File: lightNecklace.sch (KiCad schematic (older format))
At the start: 68 parts

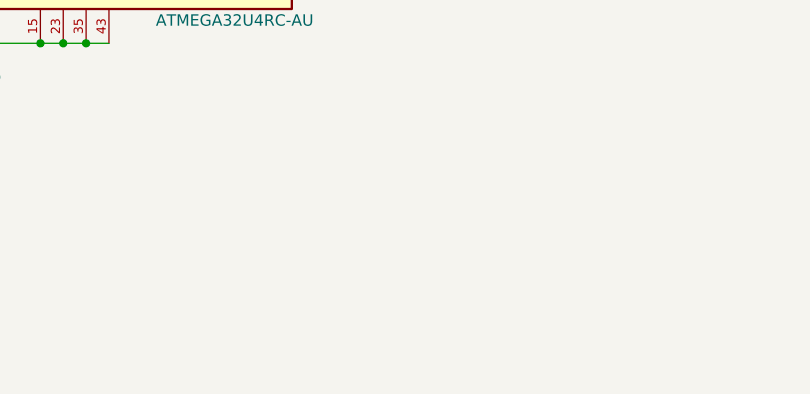
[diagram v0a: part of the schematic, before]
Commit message: Added treble cleff
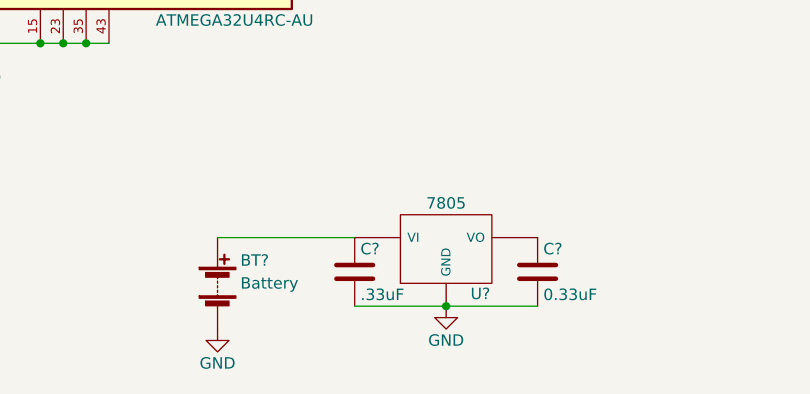
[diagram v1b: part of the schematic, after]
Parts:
- added BT?: Battery, symbol Battery
- added C?: .33uF, symbol C
- added C?: 0.33uF, symbol C
- added U?: 7805, symbol 7805
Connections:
- net GND: now also BT?.2 (-), C?.2, C?.2, U?.GND
- new net: BT?.1 (+), C?.1, U?.VI
- new net: C?.1, U?.VO
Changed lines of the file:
@@
 $EndComp
 NoConn ~ 1125 3625
-Wire Wire Line
-	1650 3325 1900 3325
-Wire Wire Line
-	1125 2925 1900 2925
-Wire Wire Line
-	1450 2625 1650 2625
-Wire Wire Line
-	1675 3025 1900 3025
-Wire Wire Line
-	1900 3025 1900 3075
-Wire Wire Line
-	1675 3225 1900 3225
-Wire Wire Line
-	1900 3225 1900 3175
-Wire Wire Line
-	2600 1475 2475 1475
-Wire Wire Line
-	2475 1475 2475 1175
-Wire Wire Line
-	2850 1475 2750 1475
-Wire Wire Line
-	2750 1475 2750 1175
-Wire Wire Line
-	2950 1475 3025 1475
-Wire Wire Line
-	3025 1475 3025 1175
-Wire Wire Line
-	3300 1475 3550 1475
-Wire Wire Line
-	3550 1475 3550 1175
-Wire Wire Line
-	2225 875  3550 875
-Connection ~ 3275 875
-Connection ~ 3025 875
-Connection ~ 2750 875
-Connection ~ 2475 875
-Connection ~ 3275 1175
-Wire Wire Line
-	3200 1475 3200 1350
-Wire Wire Line
-	3200 1350 3275 1350
-Wire Wire Line
-	3275 1350 3275 1175
-Wire Wire Line
-	3550 1175 1600 1175
-Connection ~ 3025 1175
-Connection ~ 2750 1175
-Connection ~ 2475 1175
-Wire Wire Line
-	1200 1725 1900 1725
-Wire Wire Line
-	1600 1175 1600 1425
-Connection ~ 1850 1175
-Connection ~ 1600 1725
-Wire Wire Line
-	1200 1525 1375 1525
-Wire Wire Line
-	700  1525 700  1525
-Wire Wire Line
-	700  1525 700  1350
-Wire Wire Line
-	700  1350 1375 1350
-Wire Wire Line
-	1375 1350 1375 1525
-Wire Wire Line
-	700  1725 700  1975
-Wire Wire Line
-	700  1975 1200 1975
-Wire Wire Line
-	1200 1975 1200 1725
-Wire Wire Line
-	525  2075 525  2650
-Connection ~ 525  2375
-Wire Wire Line
-	1900 2075 1900 2125
-Wire Wire Line
-	825  2075 1900 2075
-Wire Wire Line
-	1900 2375 1900 2325
-Wire Wire Line
-	825  2375 1900 2375
-Connection ~ 1175 2075
-Connection ~ 1175 2375
-Wire Wire Line
-	975  2225 525  2225
-Connection ~ 525  2225
-Wire Wire Line
-	1375 2225 1375 2175
-Wire Wire Line
-	1375 2175 1575 2175
-Wire Wire Line
-	1125 3425 1250 3425
-Wire Wire Line
-	1250 3425 1250 3025
-Wire Wire Line
-	1250 3025 1375 3025
-Wire Wire Line
-	1125 3525 1375 3525
-Wire Wire Line
-	1375 3525 1375 3225
-Wire Wire Line
-	1125 3225 1125 2925
-Connection ~ 1650 2925
-Wire Wire Line
-	725  3825 825  3825
-Connection ~ 775  3825
-Wire Wire Line
-	2650 4875 3200 4875
-Connection ~ 3000 4875
-Connection ~ 3100 4875
-Connection ~ 2900 4875
 $Comp
 L GND #PWR?
@@
 	0    1    1    0
 $EndComp
-Wire Wire Line
-	4150 1825 4600 1825
-Wire Wire Line
-	4150 1925 4600 1925
-Wire Wire Line
-	4150 2025 4600 2025
 Text Label 4150 1725 0    60   ~ 0
 LED1
@@
 Text Label 8650 4475 2    60   ~ 0
 LED25
+$Comp
+L GND #PWR?
+U 1 1 5A3F89C4
+P 7600 4775
+F 0 "#PWR?" H 7600 4525 50  0001 C CNN
+F 1 "GND" H 7600 4625 50  0000 C CNN
+F 2 "" H 7600 4775 50  0001 C CNN
+F 3 "" H 7600 4775 50  0001 C CNN
+	1    7600 4775
+	1    0    0    -1
+$EndComp
+$Comp
+L GND #PWR?
+U 1 1 5A3FA7AA
+P 9250 4475
+F 0 "#PWR?" H 9250 4225 50  0001 C CNN
+F 1 "GND" H 9250 4325 50  0000 C CNN
+F 2 "" H 9250 4475 50  0001 C CNN
+F 3 "" H 9250 4475 50  0001 C CNN
+	1    9250 4475
+	1    0    0    -1
+$EndComp
+$Comp
+L 7805 U?
+U 1 1 5A3FDDB3
+P 4675 5775
+F 0 "U?" H 4825 5579 50  0000 C CNN
+F 1 "7805" H 4675 5975 50  0000 C CNN
+F 2 "" H 4675 5775 50  0001 C CNN
+F 3 "" H 4675 5775 50  0001 C CNN
+	1    4675 5775
+	1    0    0    -1
+$EndComp
+$Comp
+L Battery BT?
+U 1 1 5A3FE745
+P 3675 5925
+F 0 "BT?" H 3775 6025 50  0000 L CNN
+F 1 "Battery" H 3775 5925 50  0000 L CNN
+F 2 "" V 3675 5985 50  0001 C CNN
+F 3 "" V 3675 5985 50  0001 C CNN
+	1    3675 5925
+	1    0    0    -1
+$EndComp
+$Comp
+L C C?
+U 1 1 5A3FEA3A
+P 4275 5875
+F 0 "C?" H 4300 5975 50  0000 L CNN
+F 1 ".33uF" H 4300 5775 50  0000 L CNN
+F 2 "" H 4313 5725 50  0001 C CNN
+F 3 "" H 4275 5875 50  0001 C CNN
+	1    4275 5875
+	1    0    0    -1
+$EndComp
+$Comp
+L C C?
+U 1 1 5A3FEB31
+P 5075 5875
+F 0 "C?" H 5100 5975 50  0000 L CNN
+F 1 "0.33uF" H 5100 5775 50  0000 L CNN
+F 2 "" H 5113 5725 50  0001 C CNN
+F 3 "" H 5075 5875 50  0001 C CNN
+	1    5075 5875
+	1    0    0    -1
+$EndComp
+$Comp
+L GND #PWR?
+U 1 1 5A4001D3
+P 4675 6025
+F 0 "#PWR?" H 4675 5775 50  0001 C CNN
+F 1 "GND" H 4675 5875 50  0000 C CNN
+F 2 "" H 4675 6025 50  0001 C CNN
+F 3 "" H 4675 6025 50  0001 C CNN
+	1    4675 6025
+	1    0    0    -1
+$EndComp
+$Comp
+L GND #PWR?
+U 1 1 5A40034F
+P 3675 6125
+F 0 "#PWR?" H 3675 5875 50  0001 C CNN
+F 1 "GND" H 3675 5975 50  0000 C CNN
+F 2 "" H 3675 6125 50  0001 C CNN
+F 3 "" H 3675 6125 50  0001 C CNN
+	1    3675 6125
+	1    0    0    -1
+$EndComp
+Wire Wire Line
+	1650 3325 1900 3325
+Wire Wire Line
+	1125 2925 1900 2925
+Wire Wire Line
+	1450 2625 1650 2625
+Wire Wire Line
+	1675 3025 1900 3025
+Wire Wire Line
+	1900 3025 1900 3075
+Wire Wire Line
+	1675 3225 1900 3225
+Wire Wire Line
+	1900 3225 1900 3175
+Wire Wire Line
+	2600 1475 2475 1475
+Wire Wire Line
+	2475 1475 2475 1175
+Wire Wire Line
+	2850 1475 2750 1475
+Wire Wire Line
+	2750 1475 2750 1175
+Wire Wire Line
+	2950 1475 3025 1475
+Wire Wire Line
+	3025 1475 3025 1175
+Wire Wire Line
+	3300 1475 3550 1475
+Wire Wire Line
+	3550 1475 3550 1175
+Wire Wire Line
+	2225 875  3550 875
+Connection ~ 3275 875
+Connection ~ 3025 875
+Connection ~ 2750 875
+Connection ~ 2475 875
+Connection ~ 3275 1175
+Wire Wire Line
+	3200 1475 3200 1350
+Wire Wire Line
+	3200 1350 3275 1350
+Wire Wire Line
+	3275 1350 3275 1175
+Wire Wire Line
+	3550 1175 1600 1175
+Connection ~ 3025 1175
+Connection ~ 2750 1175
+Connection ~ 2475 1175
+Wire Wire Line
+	1200 1725 1900 1725
+Wire Wire Line
+	1600 1175 1600 1425
+Connection ~ 1850 1175
+Connection ~ 1600 1725
+Wire Wire Line
+	1200 1525 1375 1525
+Wire Wire Line
+	700  1525 700  1525
+Wire Wire Line
+	700  1525 700  1350
+Wire Wire Line
+	700  1350 1375 1350
+Wire Wire Line
+	1375 1350 1375 1525
+Wire Wire Line
+	700  1725 700  1975
+Wire Wire Line
+	700  1975 1200 1975
+Wire Wire Line
+	1200 1975 1200 1725
+Wire Wire Line
+	525  2075 525  2650
+Connection ~ 525  2375
+Wire Wire Line
+	1900 2075 1900 2125
+Wire Wire Line
+	825  2075 1900 2075
+Wire Wire Line
+	1900 2375 1900 2325
+Wire Wire Line
+	825  2375 1900 2375
+Connection ~ 1175 2075
+Connection ~ 1175 2375
+Wire Wire Line
+	975  2225 525  2225
+Connection ~ 525  2225
+Wire Wire Line
+	1375 2225 1375 2175
+Wire Wire Line
+	1375 2175 1575 2175
+Wire Wire Line
+	1125 3425 1250 3425
+Wire Wire Line
+	1250 3425 1250 3025
+Wire Wire Line
+	1250 3025 1375 3025
+Wire Wire Line
+	1125 3525 1375 3525
+Wire Wire Line
+	1375 3525 1375 3225
+Wire Wire Line
+	1125 3225 1125 2925
+Connection ~ 1650 2925
+Wire Wire Line
+	725  3825 825  3825
+Connection ~ 775  3825
+Wire Wire Line
+	2650 4875 3200 4875
+Connection ~ 3000 4875
+Connection ~ 3100 4875
+Connection ~ 2900 4875
+Wire Wire Line
+	4150 1825 4600 1825
+Wire Wire Line
+	4150 1925 4600 1925
+Wire Wire Line
+	4150 2025 4600 2025
 Wire Wire Line
 	7600 1475 7600 4775
@@
 Connection ~ 7600 4225
 Connection ~ 7600 4500
-$Comp
-L GND #PWR?
-U 1 1 5A3F89C4
-P 7600 4775
-F 0 "#PWR?" H 7600 4525 50  0001 C CNN
-F 1 "GND" H 7600 4625 50  0000 C CNN
-F 2 "" H 7600 4775 50  0001 C CNN
-F 3 "" H 7600 4775 50  0001 C CNN
-	1    7600 4775
-	1    0    0    -1
-$EndComp
 Wire Wire Line
 	9250 1450 9250 4475
@@
 Connection ~ 9250 3925
 Connection ~ 9250 4200
-$Comp
-L GND #PWR?
-U 1 1 5A3FA7AA
-P 9250 4475
-F 0 "#PWR?" H 9250 4225 50  0001 C CNN
-F 1 "GND" H 9250 4325 50  0000 C CNN
-F 2 "" H 9250 4475 50  0001 C CNN
-F 3 "" H 9250 4475 50  0001 C CNN
-	1    9250 4475
-	1    0    0    -1
-$EndComp
+Wire Wire Line
+	4275 6025 5075 6025
+Connection ~ 4675 6025
+Wire Wire Line
+	3675 5725 4275 5725
 $EndSCHEMATC

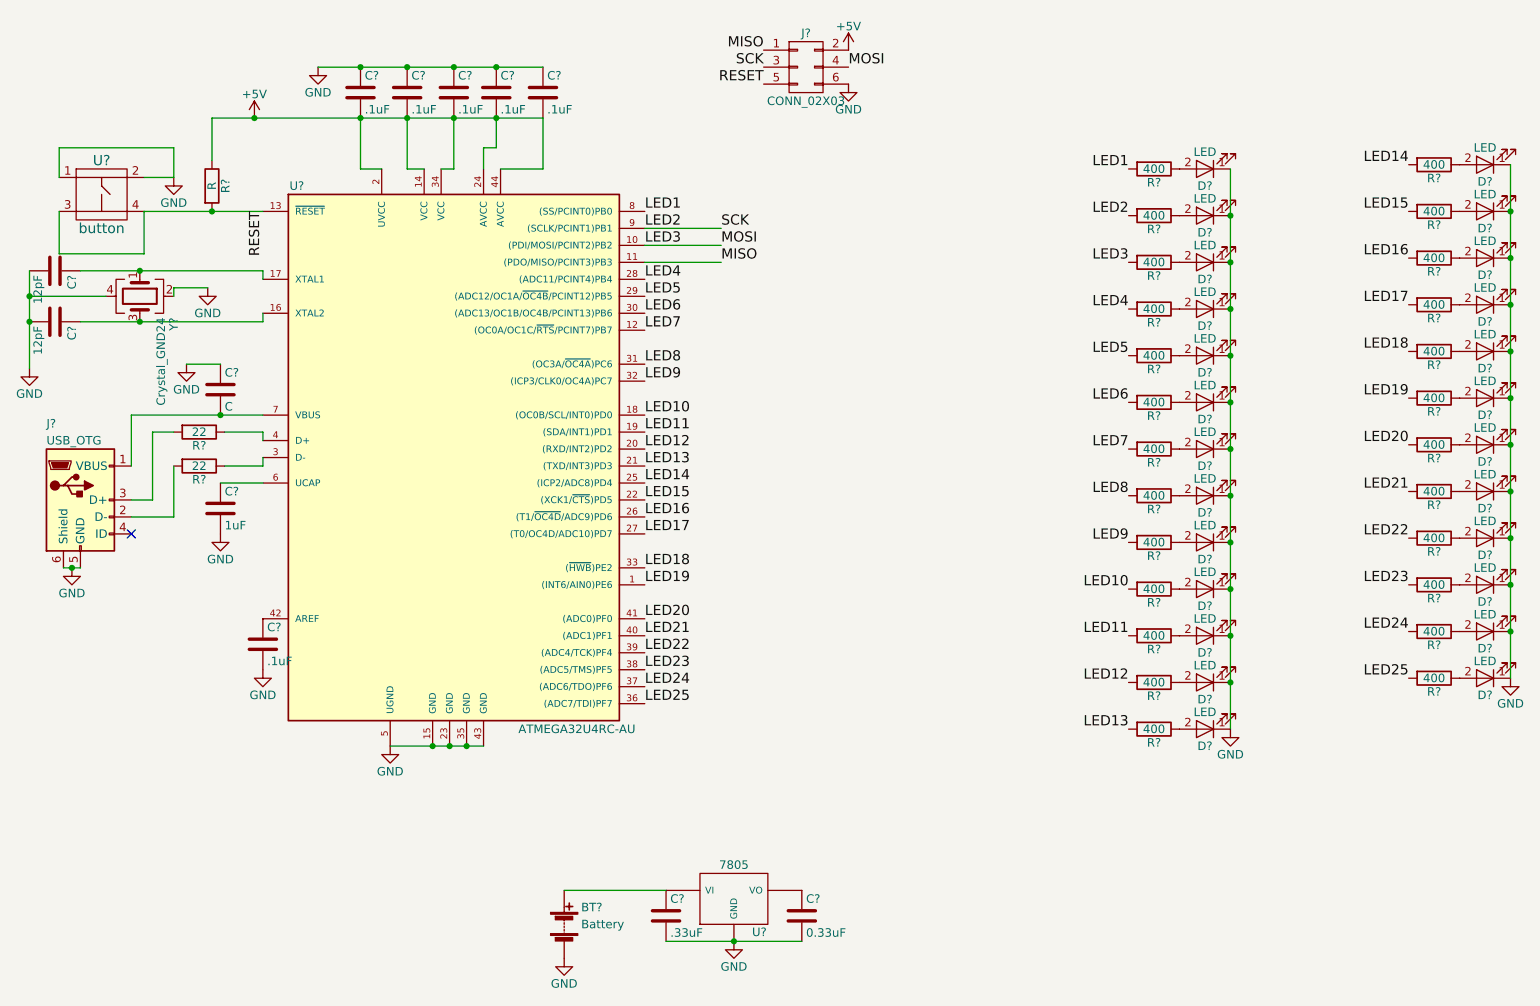
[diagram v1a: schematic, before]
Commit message: Finished CVPCB
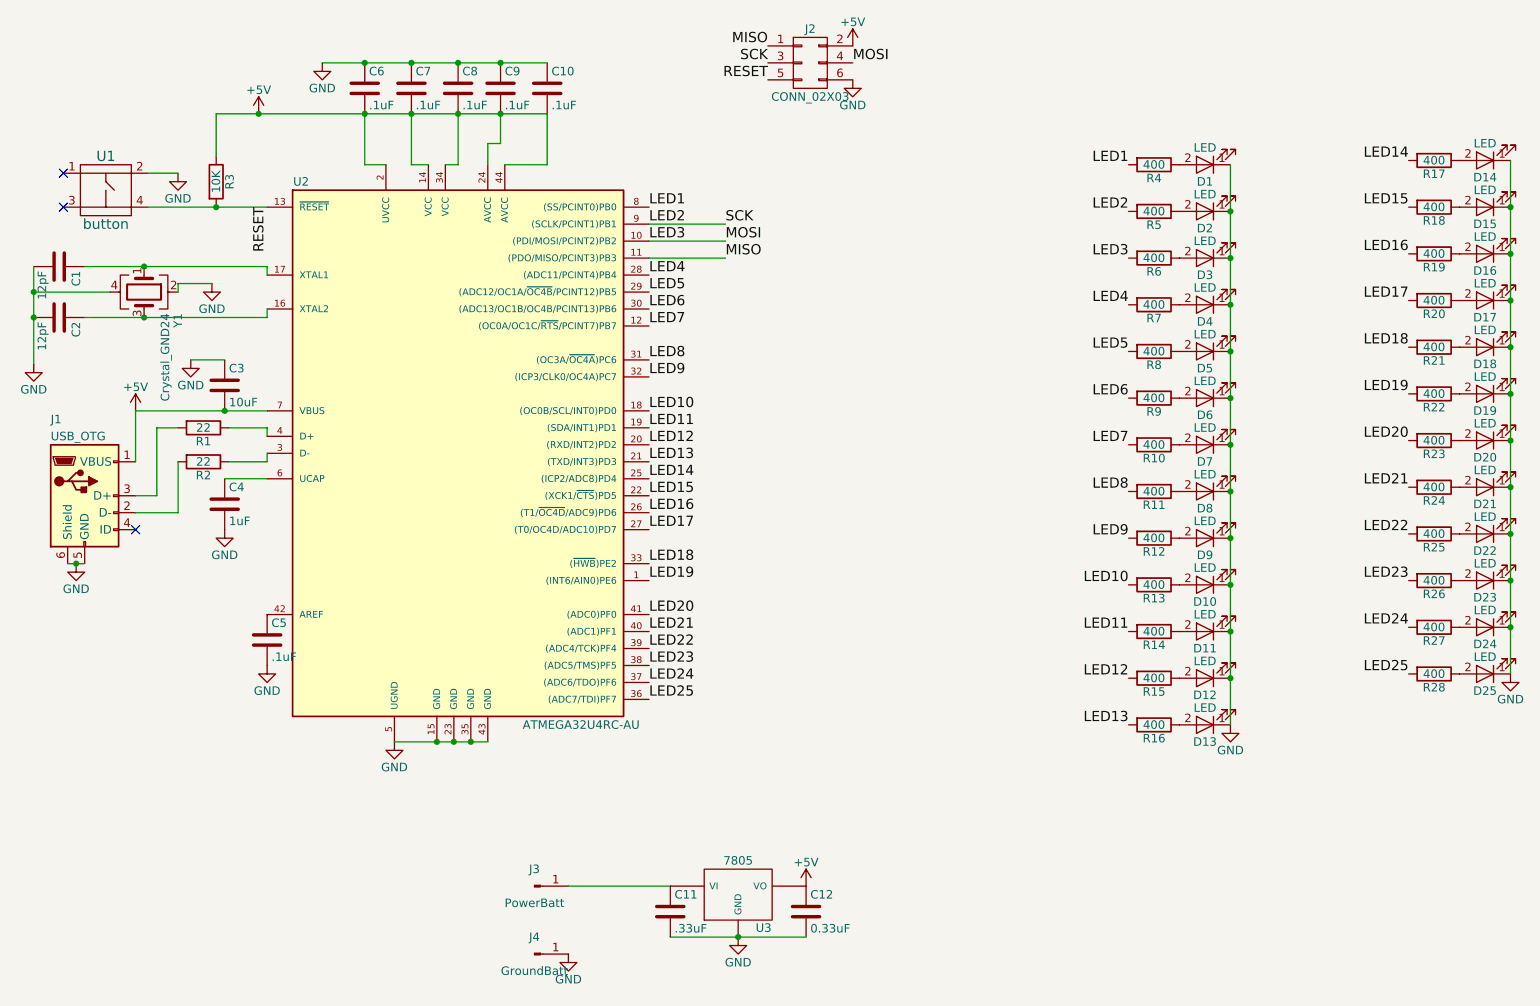
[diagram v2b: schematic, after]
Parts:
- removed BT?: Battery, symbol Battery
- added J3: PowerBatt, Connectors:1pin, symbol Conn_01x01_Male
- added J4: GroundBatt, Connectors:1pin, symbol Conn_01x01_Male
- C1, C10, C11, C12, C2, C4, C5, C6, C7, C8, C9: renamed from C?; footprint (none) -> Capacitors_SMD:C_0603
- C3: renamed from C?; value C -> 10uF; footprint (none) -> Capacitors_SMD:C_0805
- D1, D10, D11, D12, D13, D14, D15, D16, D17, D18, D19, D2, D20, D21, D22, D23, D24, D25, D3, D4, D5, D6, D7, D8, D9: renamed from D?; footprint (none) -> LEDs:LED_0805
- J1: renamed from J?; footprint (none) -> Connectors:USB_Micro-B
- J2: renamed from J?; footprint (none) -> Pin_Headers:Pin_Header_Straight_2x03_Pitch2.54mm_SMD
- R1, R10, R11, R12, R13, R14, R15, R16, R17, R18, R19, R2, R20, R21, R22, R23, R24, R25, R26, R27, R28, R4, R5, R6, R7, R8, R9: renamed from R?; footprint (none) -> Resistors_SMD:R_0603
- R3: renamed from R?; value R -> 10K; footprint (none) -> Resistors_SMD:R_0603
- U1: renamed from U?; footprint (none) -> BashPCB:KMT071_NGJ_LHS
- U2: renamed from U?; footprint TQFP44 -> Housings_QFP:TQFP-44_10x10mm_Pitch0.8mm
- U3: renamed from U?; footprint (none) -> BashPCB:D2PAK
- Y1: renamed from Y?; footprint (none) -> Crystals:Crystal_SMD_3225-4pin_3.2x2.5mm
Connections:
- net +5V: now also C12.1, C3.2, J1.1 (VBUS), U2.7 (VBUS), U3.VO
- net GND: now also J4.1 (Pin_1); no longer U1.1
- net RESET: no longer U1.3
- net at C11.1, U3.VI: now also J3.1 (Pin_1)
- no-connect marks 1 -> 3
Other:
- moved on the sheet: C1, C10, C11, C12, C2, C3, C4, C5, C6, C7, C8, C9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

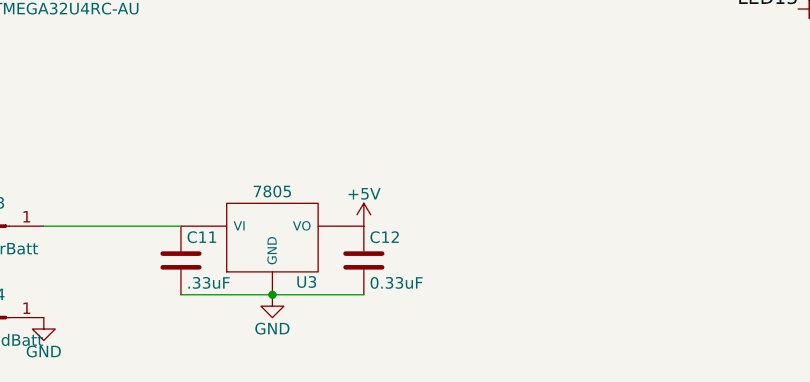
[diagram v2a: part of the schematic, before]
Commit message: Made edge cuts
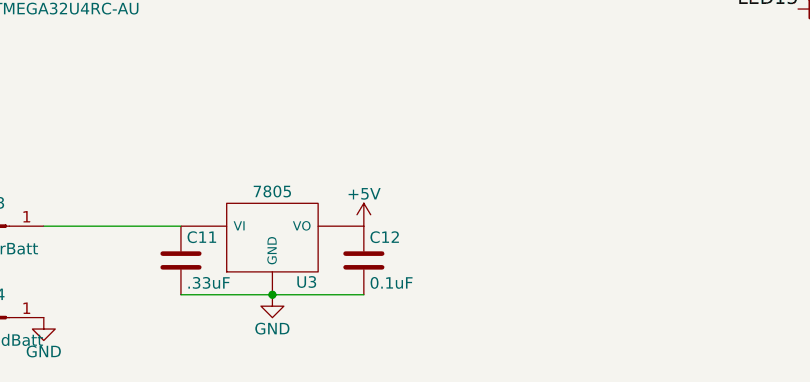
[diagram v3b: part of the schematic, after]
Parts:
- C12: value 0.33uF -> 0.1uF
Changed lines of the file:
@@
 $EndComp
 $Comp
-L GND #PWR7
+L GND #PWR01
 U 1 1 5A3D2EC8
 P 1675 3600
-F 0 "#PWR7" H 1675 3350 50  0001 C CNN
+F 0 "#PWR01" H 1675 3350 50  0001 C CNN
 F 1 "GND" H 1675 3450 50  0000 C CNN
 F 2 "" H 1675 3600 50  0001 C CNN
@@
 $EndComp
 $Comp
-L GND #PWR5
+L GND #PWR02
 U 1 1 5A3D2F7F
 P 1475 2600
-F 0 "#PWR5" H 1475 2350 50  0001 C CNN
+F 0 "#PWR02" H 1475 2350 50  0001 C CNN
 F 1 "GND" H 1475 2450 50  0000 C CNN
 F 2 "" H 1475 2600 50  0001 C CNN
@@
 $EndComp
 $Comp
-L GND #PWR10
+L GND #PWR03
 U 1 1 5A3D5EEE
 P 2250 850
-F 0 "#PWR10" H 2250 600 50  0001 C CNN
+F 0 "#PWR03" H 2250 600 50  0001 C CNN
 F 1 "GND" H 2250 700 50  0000 C CNN
 F 2 "" H 2250 850 50  0001 C CNN
@@
 $EndComp
 $Comp
-L +5V #PWR8
+L +5V #PWR04
 U 1 1 5A3DC5B9
 P 1875 1150
-F 0 "#PWR8" H 1875 1000 50  0001 C CNN
+F 0 "#PWR04" H 1875 1000 50  0001 C CNN
 F 1 "+5V" H 1875 1290 50  0000 C CNN
 F 2 "" H 1875 1150 50  0001 C CNN
@@
 $EndComp
 $Comp
-L GND #PWR4
+L GND #PWR05
 U 1 1 5A3DD2F6
 P 1400 1500
-F 0 "#PWR4" H 1400 1250 50  0001 C CNN
+F 0 "#PWR05" H 1400 1250 50  0001 C CNN
 F 1 "GND" H 1400 1350 50  0000 C CNN
 F 2 "" H 1400 1500 50  0001 C CNN
@@
 $EndComp
 $Comp
-L GND #PWR9
+L GND #PWR06
 U 1 1 5A3DEFDE
 P 1925 4400
-F 0 "#PWR9" H 1925 4150 50  0001 C CNN
+F 0 "#PWR06" H 1925 4150 50  0001 C CNN
 F 1 "GND" H 1925 4250 50  0000 C CNN
 F 2 "" H 1925 4400 50  0001 C CNN
@@
 $EndComp
 $Comp
-L GND #PWR1
+L GND #PWR07
 U 1 1 5A3DF865
 P 550 2625
-F 0 "#PWR1" H 550 2375 50  0001 C CNN
+F 0 "#PWR07" H 550 2375 50  0001 C CNN
 F 1 "GND" H 550 2475 50  0000 C CNN
 F 2 "" H 550 2625 50  0001 C CNN
@@
 $EndComp
 $Comp
-L GND #PWR6
+L GND #PWR08
 U 1 1 5A3DFA39
 P 1600 2150
-F 0 "#PWR6" H 1600 1900 50  0001 C CNN
+F 0 "#PWR08" H 1600 1900 50  0001 C CNN
 F 1 "GND" H 1600 2000 50  0000 C CNN
 F 2 "" H 1600 2150 50  0001 C CNN
@@
 $EndComp
 $Comp
-L GND #PWR2
+L GND #PWR09
 U 1 1 5A3E0520
 P 800 3800
-F 0 "#PWR2" H 800 3550 50  0001 C CNN
+F 0 "#PWR09" H 800 3550 50  0001 C CNN
 F 1 "GND" H 800 3650 50  0000 C CNN
 F 2 "" H 800 3800 50  0001 C CNN
@@
 NoConn ~ 1150 3600
 $Comp
-L GND #PWR11
+L GND #PWR010
 U 1 1 5A3E1071
 P 2675 4850
-F 0 "#PWR11" H 2675 4600 50  0001 C CNN
+F 0 "#PWR010" H 2675 4600 50  0001 C CNN
 F 1 "GND" H 2675 4700 50  0000 C CNN
 F 2 "" H 2675 4850 50  0001 C CNN
@@
 $EndComp
 $Comp
-L +5V #PWR15
+L +5V #PWR011
 U 1 1 5A3E1CAB
 P 5375 750
-F 0 "#PWR15" H 5375 600 50  0001 C CNN
+F 0 "#PWR011" H 5375 600 50  0001 C CNN
 F 1 "+5V" H 5375 890 50  0000 C CNN
 F 2 "" H 5375 750 50  0001 C CNN
@@
 $EndComp
 $Comp
-L GND #PWR16
+L GND #PWR012
 U 1 1 5A3E1DF1
 P 5375 950
-F 0 "#PWR16" H 5375 700 50  0001 C CNN
+F 0 "#PWR012" H 5375 700 50  0001 C CNN
 F 1 "GND" H 5375 800 50  0000 C CNN
 F 2 "" H 5375 950 50  0001 C CNN
@@
 LED25
 $Comp
-L GND #PWR17
+L GND #PWR013
 U 1 1 5A3F89C4
 P 7600 4750
-F 0 "#PWR17" H 7600 4500 50  0001 C CNN
+F 0 "#PWR013" H 7600 4500 50  0001 C CNN
 F 1 "GND" H 7600 4600 50  0000 C CNN
 F 2 "" H 7600 4750 50  0001 C CNN
@@
 $EndComp
 $Comp
-L GND #PWR18
+L GND #PWR014
 U 1 1 5A3FA7AA
 P 9250 4450
-F 0 "#PWR18" H 9250 4200 50  0001 C CNN
+F 0 "#PWR014" H 9250 4200 50  0001 C CNN
 F 1 "GND" H 9250 4300 50  0000 C CNN
 F 2 "" H 9250 4450 50  0001 C CNN
@@
 P 5100 5850
 F 0 "C12" H 5125 5950 50  0000 L CNN
-F 1 "0.33uF" H 5125 5750 50  0000 L CNN
+F 1 "0.1uF" H 5125 5750 50  0000 L CNN
 F 2 "Capacitors_SMD:C_0603" H 5138 5700 50  0001 C CNN
 F 3 "" H 5100 5850 50  0001 C CNN
@@
 $EndComp
 $Comp
-L GND #PWR13
+L GND #PWR015
 U 1 1 5A4001D3
 P 4700 6000
-F 0 "#PWR13" H 4700 5750 50  0001 C CNN
+F 0 "#PWR015" H 4700 5750 50  0001 C CNN
 F 1 "GND" H 4700 5850 50  0000 C CNN
 F 2 "" H 4700 6000 50  0001 C CNN
@@
 $EndComp
 $Comp
-L GND #PWR12
+L GND #PWR016
 U 1 1 5A40034F
 P 3700 6100
-F 0 "#PWR12" H 3700 5850 50  0001 C CNN
+F 0 "#PWR016" H 3700 5850 50  0001 C CNN
 F 1 "GND" H 3700 5950 50  0000 C CNN
 F 2 "" H 3700 6100 50  0001 C CNN
@@
 $EndComp
 $Comp
-L +5V #PWR3
+L +5V #PWR017
 U 1 1 5A3EEE98
 P 1150 2900
-F 0 "#PWR3" H 1150 2750 50  0001 C CNN
+F 0 "#PWR017" H 1150 2750 50  0001 C CNN
 F 1 "+5V" H 1150 3040 50  0000 C CNN
 F 2 "" H 1150 2900 50  0001 C CNN
@@
 $EndComp
 $Comp
-L +5V #PWR14
+L +5V #PWR018
 U 1 1 5A3EF6D4
 P 5100 5700
-F 0 "#PWR14" H 5100 5550 50  0001 C CNN
+F 0 "#PWR018" H 5100 5550 50  0001 C CNN
 F 1 "+5V" H 5100 5840 50  0000 C CNN
 F 2 "" H 5100 5700 50  0001 C CNN
